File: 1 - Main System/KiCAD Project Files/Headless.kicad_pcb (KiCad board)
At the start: 6 copper layers, 127 x 101.6 mm, 569 parts, among them IC1 AP22966DC8-7, IC2 AP22966DC8-7, IC3 AP22966DC8-7, IC4 AP22966DC8-7, IC5 TMUXHS221FRSWR, IC6 MAX77857CEWB+, IC7 MAX77857CEWB+, IC8 IS43TR16640C-125JBL, IC9 IS43TR16640C-125JBL, J1 Connector, USB-TYPE-C-16P, J17 PinHeader_01x01_P2.54mm_Verti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, J18 PinHeader_01x01_P2.54mm_Verti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, J2 Connector, USB-TYPE-C-16P, J3 PinSocket_01x03_P2.54mm_Verti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, J4 G97R22312HR, J5 JTAGHDR_RPi, J6 JTAGHDR_FPGA, J7 G97R22312HR, J8 G97R22312HR, J9 G97R22312HR, Q4 2N7002, Q5 T2N7002AK, Q6 T2N7002AK, SW1 SW_DIP_x03, SW2 SPDT_Slide_PTH_11.6x4.0mm, U1 MAX20029BATIA/V+, U10 ESP32-S3-WROOM-1-N4, U11 ESP32-S3-WROOM-1-N4, U12 ACS711xEXLT-15AB, U13 ACS711xEXLT-15AB, U14 ACS711xEXLT-15AB, U15 ACS711xEXLT-15AB, U16 ACS711xEXLT-15AB, U17 XC7Z020-1CLG484C, U18 STTH1002CB-TR, U19 MAX77789EWX+T, U2 LD39200PU33R, U20 TPS2592xx, U21 PCF8574AT, U22 TPS2592xx, U23 DSS1NB32A223Q91A, U24 TPS2592xx, U26 TPS2592xx, U28 TPS2592xx, U29 DSS1NB32A223Q91A, U3 STTH1002CB-TR, U30 STTH1002CB-TR, U31 DSS1NB32A223Q91A, U32 DSS1NB32A223Q91A, U33 DSS1NB32A223Q91A, U34 DSS1NB32A223Q91A, U35 ACS711xEXLT-15AB, U36 ACS711xEXLT-15AB, U37 ACS711xEXLT-15AB, U38 DSS1NB32A223Q91A, U39 DSS1NB32A223Q91A, U4 LD39200PU33R, U40 DSS1NB32A223Q91A, U5 LD39200PU33R, U6 LD39200PU33R, U7 ADS7830, U8 LD39200PU33R, U9 LD39200PU33R, Y1 ASDMB-xxxMHz

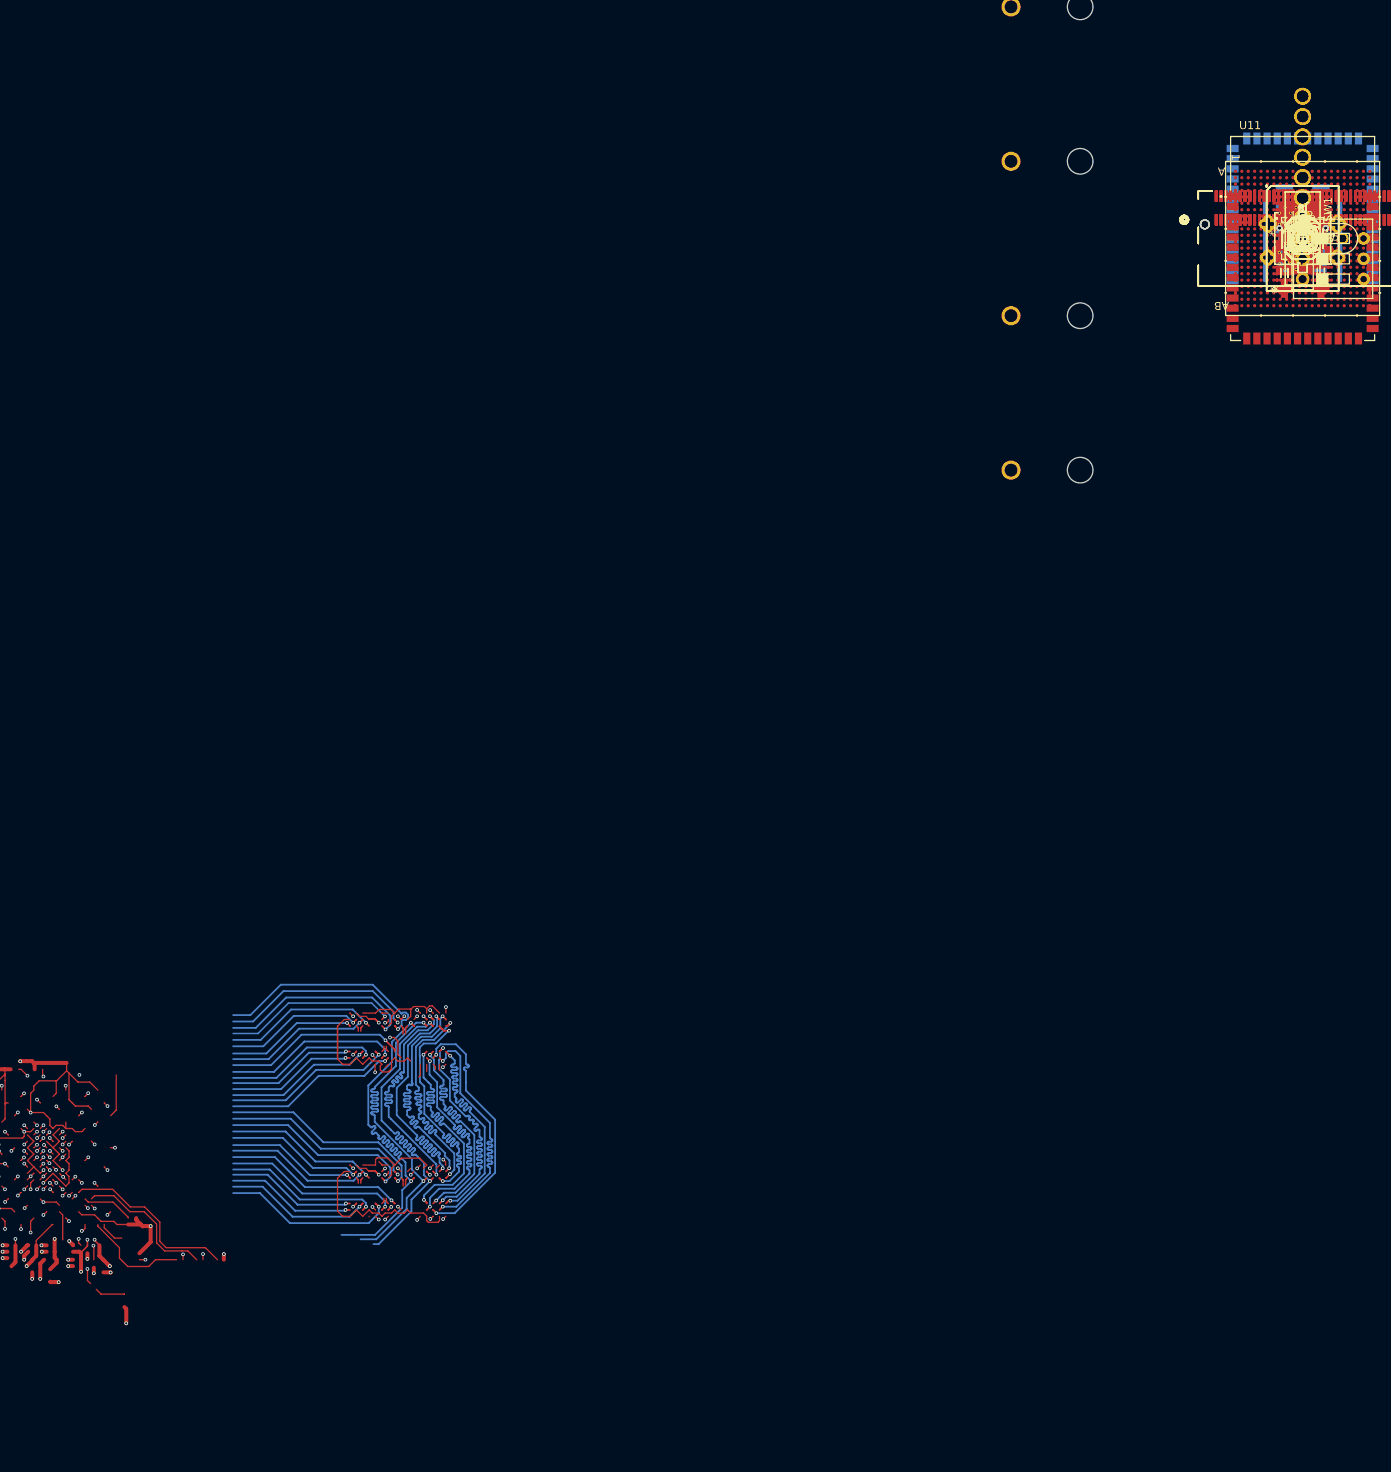
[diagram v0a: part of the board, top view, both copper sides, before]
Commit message: Routing DDR3 Completed (pre-review)
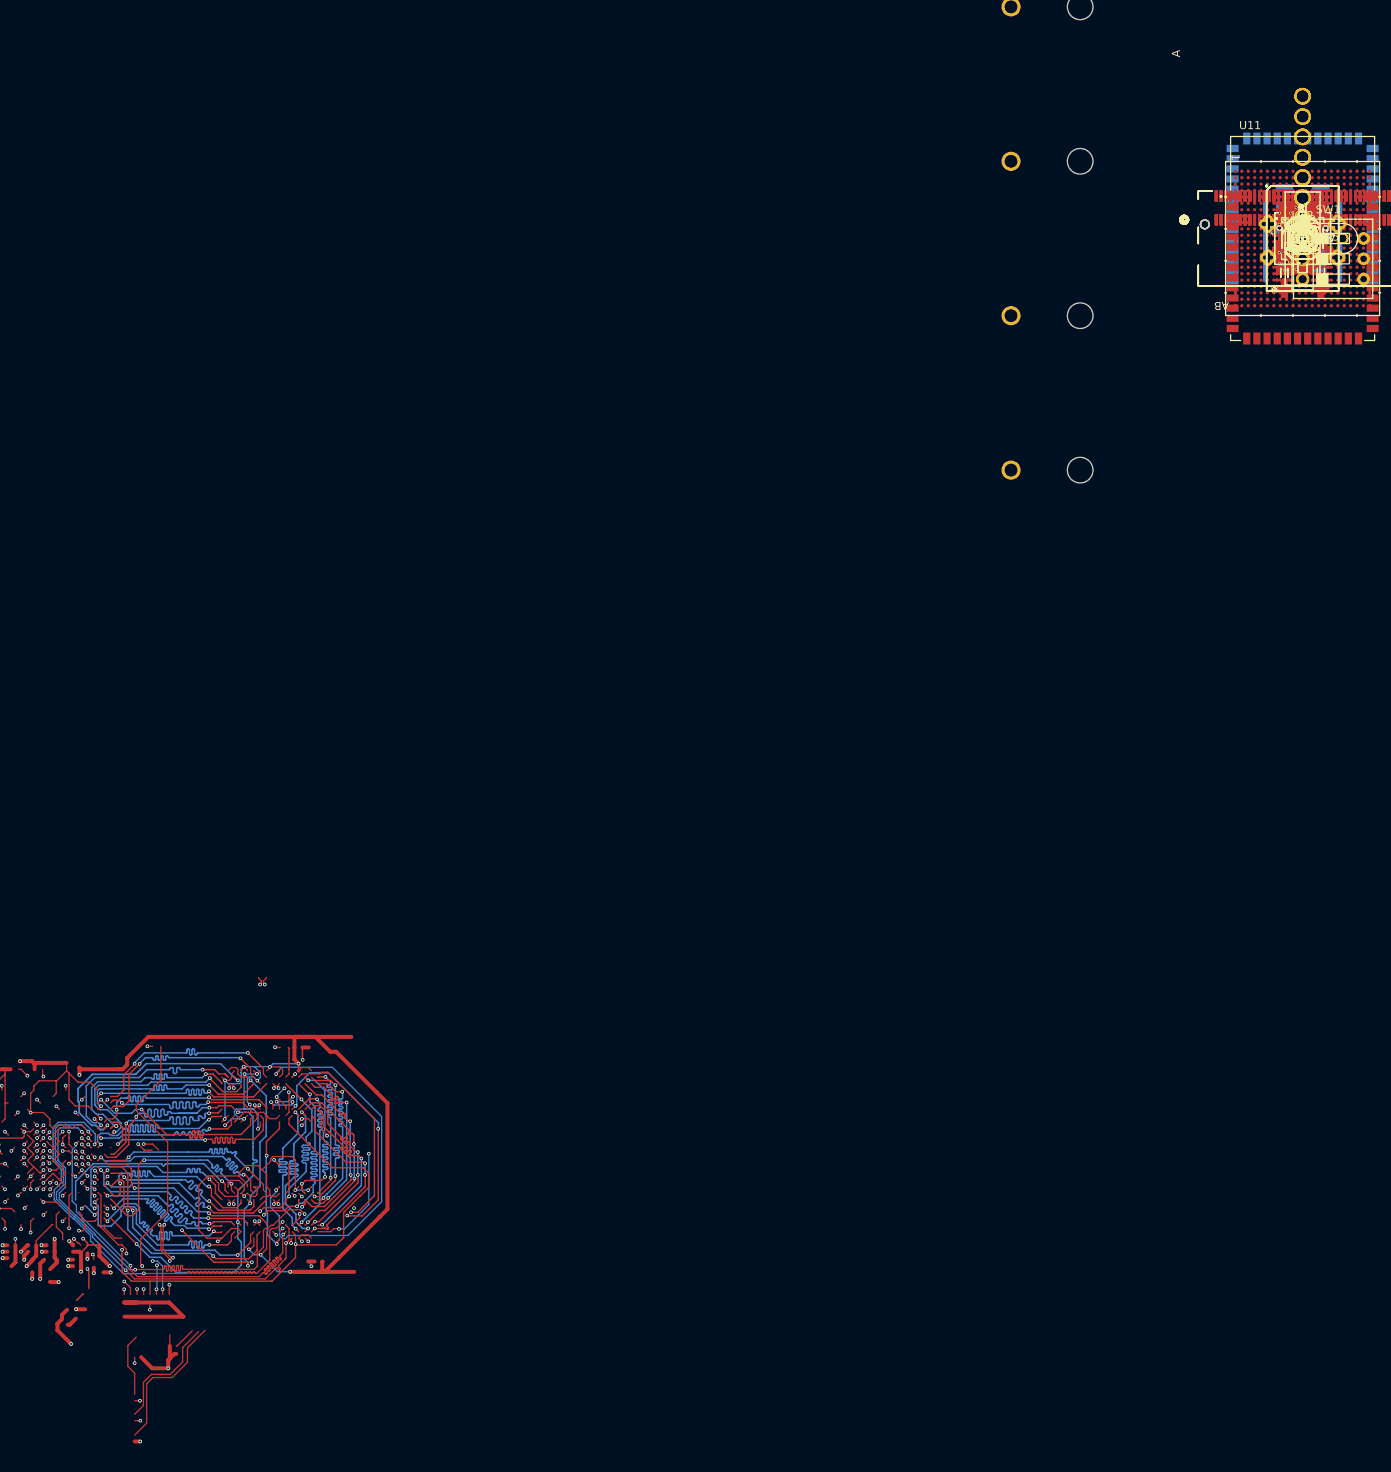
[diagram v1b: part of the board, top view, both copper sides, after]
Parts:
- added C246, C253: 22uF, PCM_JLCPCB:C_0805, F.Cu at (0.00, 0.00)
- added C247, C251, C252, C254: 4.7uF, PCM_JLCPCB:C_0805, F.Cu at (0.00, 0.00)
- added R121: 240Ω, PCM_JLCPCB:R_0402, F.Cu at (0.00, 0.00)
- added R122: 1kΩ, PCM_JLCPCB:R_0402, F.Cu at (0.00, 0.00)
- added R123: 100kΩ, PCM_JLCPCB:R_0402, F.Cu at (0.00, 0.00)
- added R124: 12kΩ, PCM_JLCPCB:R_0402, F.Cu at (0.00, 0.00)
- added U25: BD3539FVM-TR, footprints:MSOP8_ROM, F.Cu at (0.00, 0.00)
- R114: value 220Ω -> 240Ω
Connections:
- IC8 pad A1: Net-(IC8-VDDQ_1) -> +1V35FPGA
- IC8 pad A8: Net-(IC8-VDDQ_1) -> +1V35FPGA
- IC8 pad B2: Net-(IC8-VDDQ_1) -> +1V35FPGA
- IC8 pad C1: Net-(IC8-VDDQ_1) -> +1V35FPGA
- IC8 pad C9: Net-(IC8-VDDQ_1) -> +1V35FPGA
- IC8 pad D2: Net-(IC8-VDDQ_1) -> +1V35FPGA
- IC8 pad D9: Net-(IC8-VDDQ_1) -> +1V35FPGA
- IC8 pad E9: Net-(IC8-VDDQ_1) -> +1V35FPGA
- IC8 pad F1: Net-(IC8-VDDQ_1) -> +1V35FPGA
- IC8 pad F3: unconnected-(IC8-DQSL-PadF3) -> /FPGA/FPGA DDR/DQSL_P
- IC8 pad G7: Net-(IC8-VDDQ_1) -> +1V35FPGA
- IC8 pad H1: unconnected-(IC8-VREFDQ-PadH1) -> +1V35FPGA
- IC8 pad H2: Net-(IC8-VDDQ_1) -> +1V35FPGA
- IC8 pad H9: Net-(IC8-VDDQ_1) -> +1V35FPGA
- IC8 pad K2: Net-(IC8-VDDQ_1) -> +1V35FPGA
- IC8 pad K8: Net-(IC8-VDDQ_1) -> +1V35FPGA
- IC8 pad K9: unconnected-(IC8-CKE-PadK9) -> /FPGA/FPGA DDR/DDR_CKE
- IC8 pad L3: unconnected-(IC8-WE#-PadL3) -> /FPGA/FPGA DDR/DDR_WE
- IC8 pad L8: /FPGA/FPGA DDR/DDR_ZQ -> Net-(IC8-ZQ)
- IC8 pad M3: unconnected-(IC8-BA2-PadM3) -> /FPGA/FPGA DDR/DDR_BA2
- IC8 pad N1: Net-(IC8-VDDQ_1) -> +1V35FPGA
- IC8 pad N9: Net-(IC8-VDDQ_1) -> +1V35FPGA
- IC8 pad R1: Net-(IC8-VDDQ_1) -> +1V35FPGA
- IC8 pad R9: Net-(IC8-VDDQ_1) -> +1V35FPGA
- IC9 pad H1: unconnected-(IC9-VREFDQ-PadH1) -> +1V35FPGA
- IC9 pad L8: /FPGA/FPGA DDR/DDR_ZQ -> Net-(IC9-ZQ)
- R102 pad 2: unconnected-(R102-Pad2) -> /FPGA/FPGA DDR/DDR_CKP
- R114 pad 2: /FPGA/FPGA DDR/DDR_ZQ -> Net-(IC9-ZQ)
- U17 pad H7: +0V675 -> +0V675_REF
- U17 pad L4: unconnected-(U17A-PS_DDR_A3_502-PadL4) -> /FPGA/FPGA DDR/DDR_A3
- U17 pad P7: +0V675 -> +0V675_REF
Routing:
- net /FPGA/FPGA DDR/DDR_CKN: track 2.20 -> 236.6 mm, vias 0 -> 6
- net /FPGA/FPGA DDR/DDR_CKP: track 2.20 -> 235.7 mm, vias 0 -> 6
- net +1V35FPGA: track 88.9 -> 270.7 mm, vias 2 -> 18
- net /FPGA/FPGA DDR/DDR_CAS: track 0.00 -> 96.2 mm, vias 0 -> 6
- net /FPGA/FPGA DDR/DDR_WE: track 0.00 -> 94.7 mm, vias 0 -> 6
- net /FPGA/FPGA DDR/DDR_RAS: track 0.00 -> 91.5 mm, vias 0 -> 6
- net /FPGA/FPGA DDR/DDR_BA2: track 0.00 -> 91.0 mm, vias 0 -> 7
- net /FPGA/FPGA DDR/DDR_CKE: track 0.00 -> 90.2 mm, vias 0 -> 4
- net /FPGA/FPGA DDR/DDR_CS: track 0.00 -> 87.9 mm, vias 0 -> 5
- net /FPGA/FPGA DDR/DDR_BA1: track 1.15 -> 83.3 mm, vias 2 -> 5
- net /FPGA/FPGA DDR/DDR_BA0: track 0.00 -> 74.9 mm, vias 0 -> 3
- net /FPGA/FPGA DDR/DDR_nRST: track 0.00 -> 65.0 mm, vias 0 -> 4
- net /FPGA/FPGA DDR/DDR_ODT: track 0.00 -> 64.3 mm, vias 0 -> 4
- net /FPGA/FPGA DDR/DDR_DM1: track 0.00 -> 56.2 mm, vias 0 -> 4
- net +0V675: track 1.12 -> 55.7 mm
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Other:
- board text removed: "47nF"
